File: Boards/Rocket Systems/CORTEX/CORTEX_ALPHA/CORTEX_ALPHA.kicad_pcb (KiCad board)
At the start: 2 copper layers, 1 part, among them U1 NUCLEO-F302R8

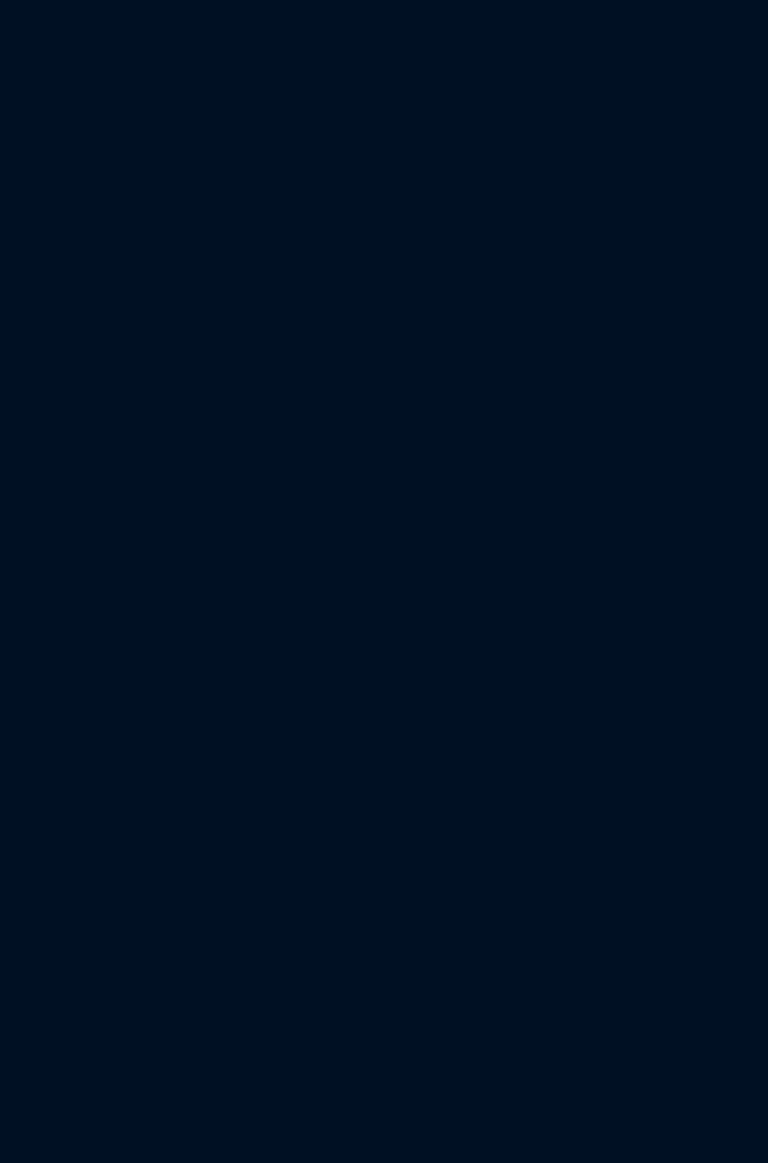
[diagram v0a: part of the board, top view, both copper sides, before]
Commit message: added radio module
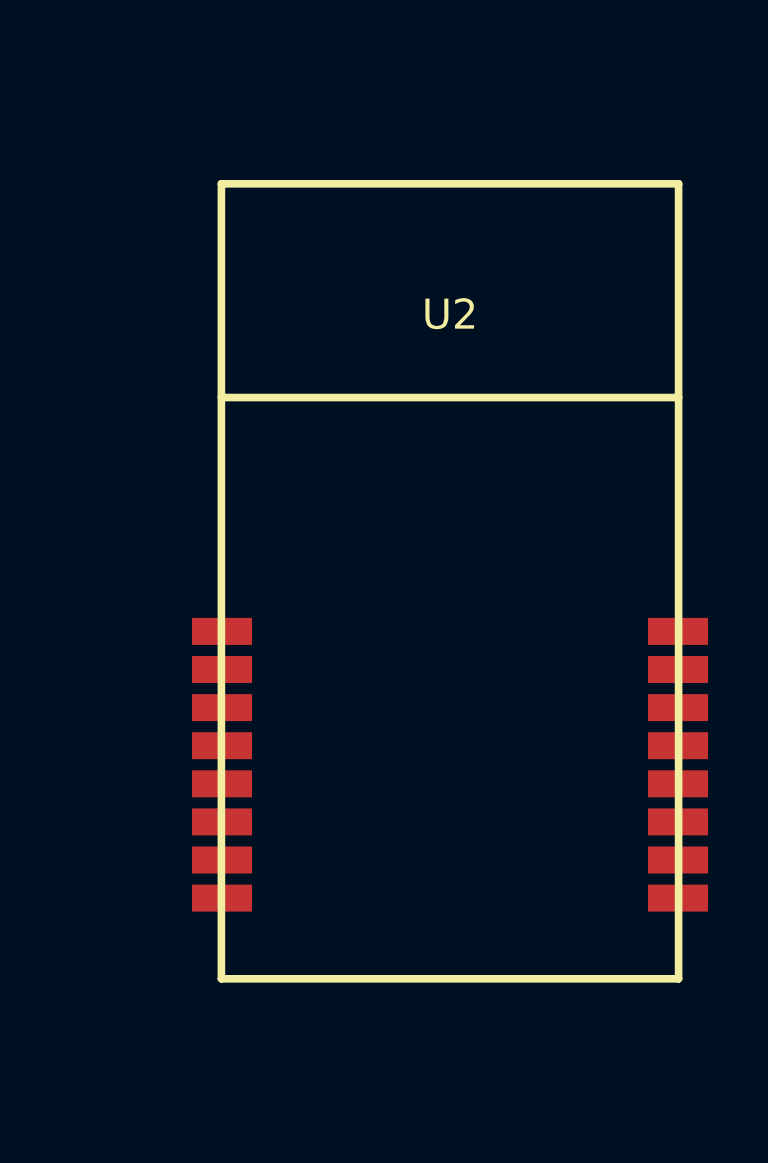
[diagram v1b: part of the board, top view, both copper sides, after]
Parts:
- added U2: E28-2G4M27S_LoRa, CORTEX:E28-2G4M27S, F.Cu at (177.5, 88.0)

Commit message: edge cuts
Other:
- board outline added: 118.5 x 92.5 mm
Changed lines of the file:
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@@
 		(embedded_fonts no)
+	)
+	(gr_rect
+		(start 81.5 39)
+		(end 200 131.5)
+		(stroke
+			(width 0.05)
+			(type default)
+		)
+		(fill no)
+		(layer "Edge.Cuts")
 	)
 	(embedded_fonts no)

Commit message: Main components placed
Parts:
- added CanBus_Module1: ~, CORTEX:Canbus, F.Cu at (175.5, 110.5)
- added U3: MAX485_MODULE_5V_LOGIC_TLL_TO_RS-485_CONVERTER, MAX485_MODULE_5V_LOGIC_TLL_TO_RS-485_CONVERTER:MODULE_MAX485_MODULE_5V_LOGIC_TLL_TO_RS-485_CONVERTER, F.Cu at (188.9, 56.2)
- added U4: ~, LIFT:MicroSD Reader, F.Cu at (199.3, 85.9)
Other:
- board size 118.5 x 92.5 mm -> 135 x 92.5 mm

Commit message: progress
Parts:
- added U5: ~, CORTEX:DCDC_Module, F.Cu at (200.3, 118.0)
- moved CanBus_Module1 2.00 mm to (173.5, 110.5)

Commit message: Cortex Update
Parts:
- added C1: 10uF, Capacitor_SMD:C_0603_1608Metric_Pad1.08x0.95mm_HandSolder, F.Cu at (120.6, 89.1)
- added C2: 47uF, Capacitor_SMD:C_0603_1608Metric_Pad1.08x0.95mm_HandSolder, F.Cu at (117.3, 89.1)
- added C3: 47uF, Capacitor_SMD:C_0603_1608Metric_Pad1.08x0.95mm_HandSolder, F.Cu at (122.1, 121.3)
- added C4: 10uF, Capacitor_SMD:C_0603_1608Metric_Pad1.08x0.95mm_HandSolder, F.Cu at (119.1, 121.3)
- added C5: 100uF, Capacitor_SMD:C_0603_1608Metric_Pad1.08x0.95mm_HandSolder, F.Cu at (147.4, 115.6)
- added C6: 0.1uF, Capacitor_SMD:C_0603_1608Metric_Pad1.08x0.95mm_HandSolder, F.Cu at (149.0, 115.5)
- added G***: LOGO, FEUP-text:Feup-text, F.Cu at (176.6, 120.1)
- added G***: LOGO, LogoPST:LogoPST, F.Cu at (112.4, 131.0)
- added J2: Screw_Terminal_01x02, TerminalBlock:TerminalBlock_Xinya_XY308-2.54-2P_1x02_P2.54mm_Horizontal, F.Cu at (104.4, 75.3)
- added J3: 1200700164, CONN_1200700164_MOL:CONN_1200700164_MOL, F.Cu at (134.5, 115.4)
- added R1: 1K, Resistor_SMD:R_0603_1608Metric_Pad0.98x0.95mm_HandSolder, F.Cu at (145.9, 66.0)
- added R2: 10K, Resistor_SMD:R_0603_1608Metric_Pad0.98x0.95mm_HandSolder, F.Cu at (169.3, 121.2)
- U1: value NUCLEO-F302R8 -> YAAJ_BluePill; footprint MyLibrary:MODULE_NUCLEO-F302R8 -> STM32 Blue Pill:YAAJ_BluePill_1
- moved U5 88.6 mm to (112.6, 105.2), turned to 90 degrees
- moved U3 66.7 mm to (122.9, 65.9)
- moved CanBus_Module1 47.0 mm to (135.9, 82.4), turned to -90 degrees
- moved U2 37.6 mm to (159.1, 120.8), turned to 180 degrees
- moved U1 36.5 mm to (152.3, 61.3)
- moved U4 17.6 mm to (181.8, 86.0), turned to -90 degrees
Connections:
- CanBus_Module1 pad 1: unconnected-(CanBus_Module1-CANL-Pad1) -> Net-(CanBus_Module1-CANL)
- CanBus_Module1 pad 2: unconnected-(CanBus_Module1-CANH-Pad2) -> Net-(CanBus_Module1-CANH)
- CanBus_Module1 pad 3: unconnected-(CanBus_Module1-CRX-Pad3) -> /CAN_RX
- CanBus_Module1 pad 4: unconnected-(CanBus_Module1-CTX-Pad4) -> /CAN_TX
- CanBus_Module1 pad 5: unconnected-(CanBus_Module1-GND-Pad5) -> GND
- CanBus_Module1 pad 6: unconnected-(CanBus_Module1-VCC-Pad6) -> +5V
- U2 pad 1: unconnected-(U2-3.3V-Pad1) -> +3.3V
- U2 pad 10: unconnected-(U2-GND-Pad10) -> GND
- U2 pad 11: unconnected-(U2-NRESET-Pad11) -> /ANT_NRESET
- U2 pad 12: unconnected-(U2-BUSY-Pad12) -> /ANT_BUSY
- U2 pad 13: unconnected-(U2-DI01-Pad13) -> /ANT_DIO1
- U2 pad 16: unconnected-(U2-GND-Pad16) -> GND
- U2 pad 2: unconnected-(U2-GND-Pad2) -> GND
- U2 pad 3: unconnected-(U2-MISO_TX-Pad3) -> /ANT_MISO
- U2 pad 4: unconnected-(U2-MOSI_RX-Pad4) -> /ANT_MOSI
- U2 pad 5: unconnected-(U2-SCK_RTS-Pad5) -> /ANT_SCK
- U2 pad 6: unconnected-(U2-NSS_CTS-Pad6) -> /ANT_NSS
- U2 pad 7: unconnected-(U2-GND-Pad7) -> GND
- U2 pad 8: unconnected-(U2-RX_EN-Pad8) -> /ANT_RX_EN
- U2 pad 9: unconnected-(U2-TX_EN-Pad9) -> /ANT_TX_EN
- U3 pad 1: unconnected-(U3-GND-Pad1) -> GND
- U3 pad 2: unconnected-(U3-A-Pad2) -> /RS_A
- U3 pad 3: unconnected-(U3-B-Pad3) -> /RS_B
- U3 pad 4: unconnected-(U3-VCC-Pad4) -> +5V
- U3 pad 5: unconnected-(U3-RO-Pad5) -> /RS_RX
- U3 pad 6: unconnected-(U3-RE-Pad6) -> /RS_ENABLE
- U3 pad 7: unconnected-(U3-DE-Pad7) -> /RS_ENABLE
- U3 pad 8: unconnected-(U3-DI-Pad8) -> /RS_TX
- U4 pad 1: unconnected-(U4-GND-Pad1) -> GND
- U4 pad 2: unconnected-(U4-MISO-Pad2) -> /SD_MISO
- U4 pad 3: unconnected-(U4-CLK-Pad3) -> /SD_CLK
- U4 pad 4: unconnected-(U4-MOSI-Pad4) -> /SD_MOSI
- U4 pad 5: unconnected-(U4-CS-Pad5) -> /SD_CS
- U4 pad 6: unconnected-(U4-3.3V-Pad6) -> +3.3V
- U5 pad 1: unconnected-(U5-IN+-Pad1) -> /+12.8V
- U5 pad 2: unconnected-(U5-IN--Pad2) -> GND
- U5 pad 3: unconnected-(U5-OUT+-Pad3) -> +5V
- U5 pad 4: unconnected-(U5-OUT--Pad4) -> GND
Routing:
- net +5V: track 0.00 -> 87.5 mm
- net /RS_A: track 0.00 -> 62.7 mm
- net /RS_B: track 0.00 -> 61.1 mm
- net /ANT_NRESET: track 0.00 -> 51.4 mm
- net /ANT_RX_EN: track 0.00 -> 49.1 mm
- net /ANT_BUSY: track 0.00 -> 47.3 mm
- net /ANT_DIO1: track 0.00 -> 45.5 mm
- net /ANT_NSS: track 0.00 -> 41.1 mm
- net Net-(CanBus_Module1-CANL): track 0.00 -> 39.1 mm
- net Net-(CanBus_Module1-CANH): track 0.00 -> 39.1 mm
- net /ANT_SCK: track 0.00 -> 37.0 mm
- net /ANT_MOSI: track 0.00 -> 35.2 mm
- net /ANT_MISO: track 0.00 -> 31.6 mm
- net /ANT_TX_EN: track 0.00 -> 30.0 mm
- net /+12.8V: track 0.00 -> 25.0 mm
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- added copper zone on F.Cu, net +3.3V
- added copper zone on B.Cu, net GND
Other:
- board size 135 x 92.5 mm -> 81 x 83 mm

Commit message: PCBs acabadas e modulo de radio feito
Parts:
- removed C5: 100uF, Capacitor_SMD:C_0603_1608Metric_Pad1.08x0.95mm_HandSolder
- removed C6: 0.1uF, Capacitor_SMD:C_0603_1608Metric_Pad1.08x0.95mm_HandSolder
- U2: footprint CORTEX:E28-2G4M27S -> Radio_Module_PST:Radio_Module_PST
- moved R2 7.08 mm to (174.1, 126.4)
- moved U2 5.82 mm to (159.6, 126.6), turned to 0 degrees
- moved G*** 1.22 mm to (177.3, 121.1)
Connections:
- U1 pad 27: unconnected-(U1-PA2-Pad27) -> /ANT_DIO1
- U1 pad 33: /ANT_DIO1 -> unconnected-(U1-PB0-Pad33)
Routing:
- net /ANT_NRESET: track 51.4 -> 65.2 mm
- net /ANT_NSS: track 41.1 -> 52.9 mm
- net /ANT_BUSY: track 47.3 -> 59.0 mm
- net /ANT_SCK: track 37.0 -> 46.7 mm
- net GND: track 21.4 -> 12.2 mm, vias 12 -> 6
- net /ANT_TX_EN: track 30.0 -> 39.2 mm
- net /ANT_DIO1: track 45.5 -> 37.7 mm
- net /ANT_MISO: track 31.6 -> 38.0 mm
- net unconnected-(U1-PB0-Pad33): track 0.00 -> 2.93 mm
- net +3.3V: track 2.56 -> 0.00 mm
- net /ANT_RX_EN: track 49.1 -> 46.7 mm
- net /ANT_MOSI: track 35.2 -> 36.9 mm

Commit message: Cortex FIM
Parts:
- removed the G*** at (112.4, 131.0)
- removed U1: YAAJ_BluePill, STM32 Blue Pill:YAAJ_BluePill_1
- added J1: Conn_01x06_Pin, Connector_PinSocket_2.54mm:PinSocket_1x06_P2.54mm_Vertical, B.Cu at (121.6, 137.5)
- added J4: Conn_01x06_Pin, Connector_PinSocket_2.54mm:PinSocket_1x06_P2.54mm_Vertical, F.Cu at (178.0, 76.9)
- J3: footprint CONN_1200700164_MOL:CONN_1200700164_MOL -> 1200700164_MOL:CONN_1200700164_MOL
- U4: value ~ -> NUCLEO-G431KB; footprint LIFT:MicroSD Reader -> NUCLEO_G431KB:MODULE_NUCLEO-G431KB
- moved U4 21.2 mm to (160.6, 85.5), turned to 0 degrees
- moved R1 2.06 mm to (145.9, 64.0), turned to 90 degrees
- moved G*** 0.31 mm to (177.6, 121.1)
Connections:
- U2 pad 3: /ANT_MISO -> /MISO
- U2 pad 4: /ANT_MOSI -> /MOSI
- U2 pad 5: /ANT_SCK -> /CLK
- U2 pad 6: /ANT_NSS -> /CS
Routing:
- net /CS: track 0.00 -> 73.1 mm
- net /CLK: track 0.00 -> 69.7 mm
- net /ANT_NRESET: track 65.2 -> 0.00 mm
- net /MOSI: track 0.00 -> 63.9 mm
- net /MISO: track 0.00 -> 63.1 mm
- net /ANT_BUSY: track 59.0 -> 0.00 mm
- net +5V: track 87.5 -> 140.7 mm
- net /ANT_NSS: track 52.9 -> 0.02 mm
- net /ANT_SCK: track 46.7 -> 0.00 mm
- net /ANT_MISO: track 38.0 -> 0.00 mm
- net /ANT_MOSI: track 36.9 -> 0.00 mm
- net GND: track 12.2 -> 28.6 mm
- net /CAN_RX: track 9.55 -> 24.9 mm
- net /RS_ENABLE: track 24.4 -> 35.6 mm
- net /SD_MOSI: track 9.69 -> 0.00 mm
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
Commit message: cortex
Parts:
- added G***: LOGO, Eurocircuits:LogoEurocircuits, F.Cu at (111.1, 127.9)
- added G***: LOGO, LogoPST:LogoPST, F.Cu at (136.5, 98.3)
- added REF**: MountingHole_3.2mm_M3_DIN965, MountingHole:MountingHole_3.2mm_M3_DIN965, F.Cu at (95.4, 130.4)
- added REF**: MountingHole_3.2mm_M3_DIN965, MountingHole:MountingHole_3.2mm_M3_DIN965, F.Cu at (95.4, 69.4)
- added REF**: MountingHole_3.2mm_M3_DIN965, MountingHole:MountingHole_3.2mm_M3_DIN965, F.Cu at (185.4, 130.5)
- added REF**: MountingHole_3.2mm_M3_DIN965, MountingHole:MountingHole_3.2mm_M3_DIN965, F.Cu at (185.4, 69.6)
- J4: moved to B.Cu
- turned J4 to 180 degrees
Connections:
- U4 pad CN4_6: /ANT_NSS -> /ANT_BUSY
- U4 pad CN4_7: /ANT_SCK -> /ANT_NRESET
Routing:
- net /ANT_BUSY: track 0.00 -> 53.6 mm
- net /ANT_NRESET: track 0.00 -> 53.6 mm
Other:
- board size 81 x 83 mm -> 97.1 x 83 mm
- board text added: "CORTEX"
